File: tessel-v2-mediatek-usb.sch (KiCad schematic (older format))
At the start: 35 parts, among them J901 USB_A_2_stack, U201 MT7620N, U901 AIC1528-0PSTR, U903 FE1.1, X901 12MHz

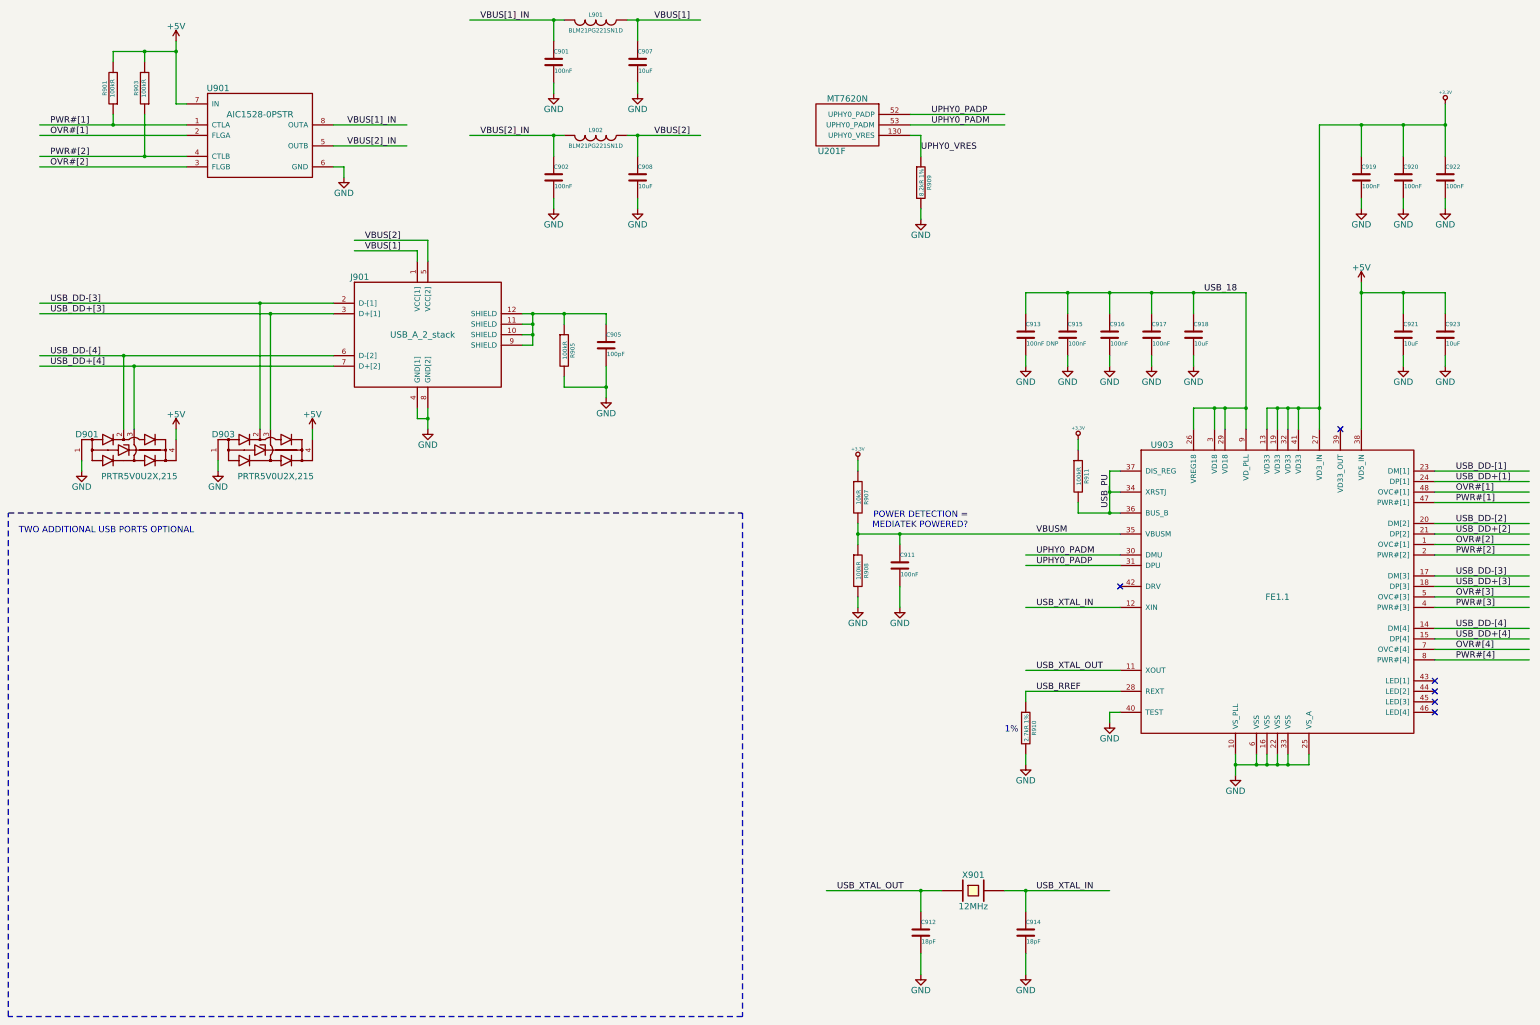
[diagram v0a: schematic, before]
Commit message: 1) can't believe i started from scratch 2) single best feature in today's kicad build: allign/distribute.
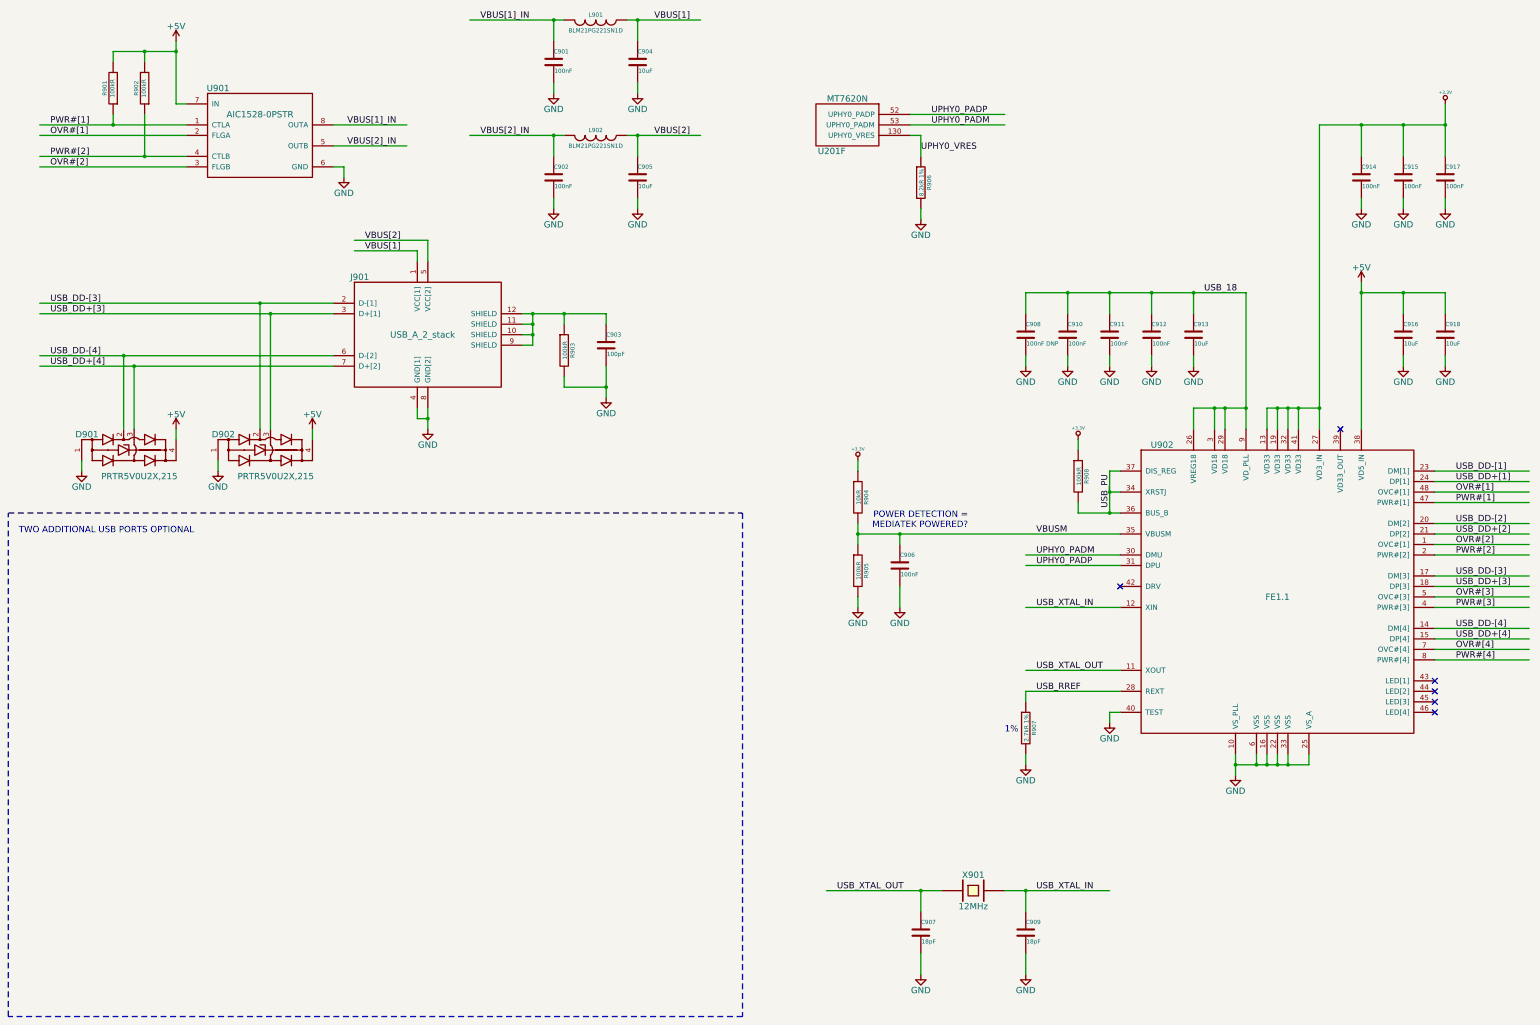
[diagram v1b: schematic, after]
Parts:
- renumbered C905 to C903, C907 to C904, C908 to C905, C911 to C906, C912 to C907, C913 to C908, C914 to C909, C915 to C910, C916 to C911, C917 to C912, C918 to C913, C919 to C914, C920 to C915, C921 to C916, C922 to C917, C923 to C918, D903 to D902, R903 to R902, R905 to R903, R907 to R904, R908 to R905, R909 to R906, R910 to R907, R911 to R908, U903 to U902

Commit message: sadly, we may need to rotate the mediatek...
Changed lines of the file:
@@
 $EndComp
 Text Label 1400 3600 0    60   ~ 0
-USB_DD-[3]
+USB_DD-[1]
 Text Label 1400 3700 0    60   ~ 0
-USB_DD+[3]
+USB_DD+[1]
 Text Label 1400 4100 0    60   ~ 0
-USB_DD-[4]
+USB_DD-[2]
 Text Label 1400 4200 0    60   ~ 0
-USB_DD+[4]
+USB_DD+[2]
 $Comp
 L PRTR5V0U2X,215 D901

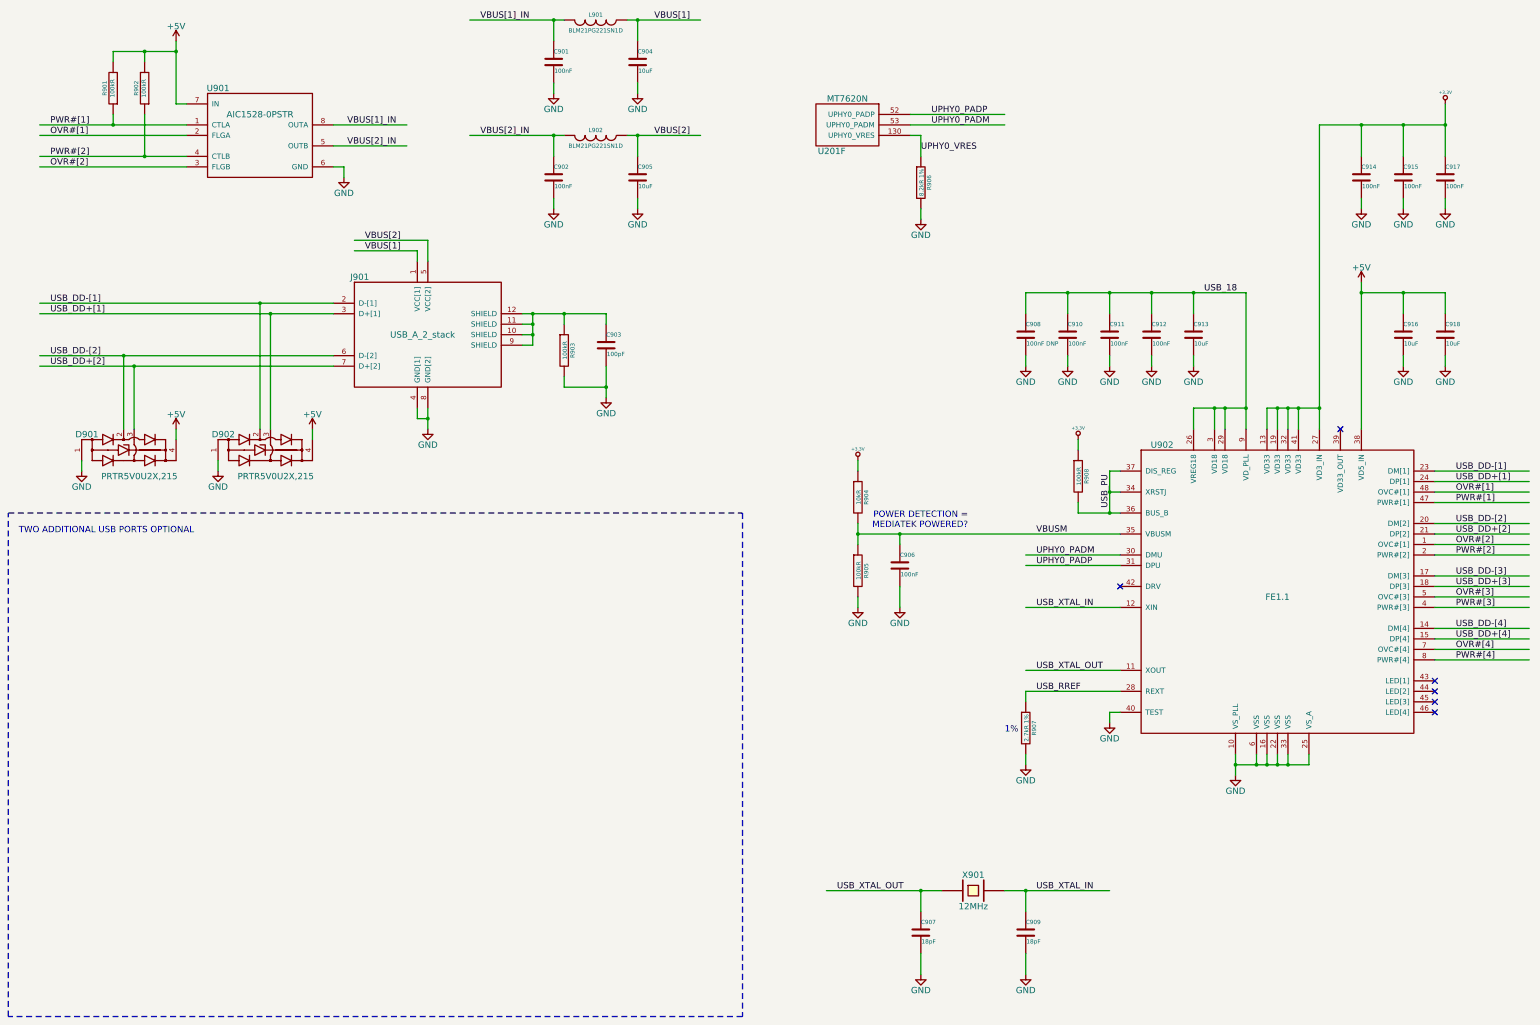
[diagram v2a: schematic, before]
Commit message: changes to usb domain: enable 3V3 reg, tie vbusm to mt33
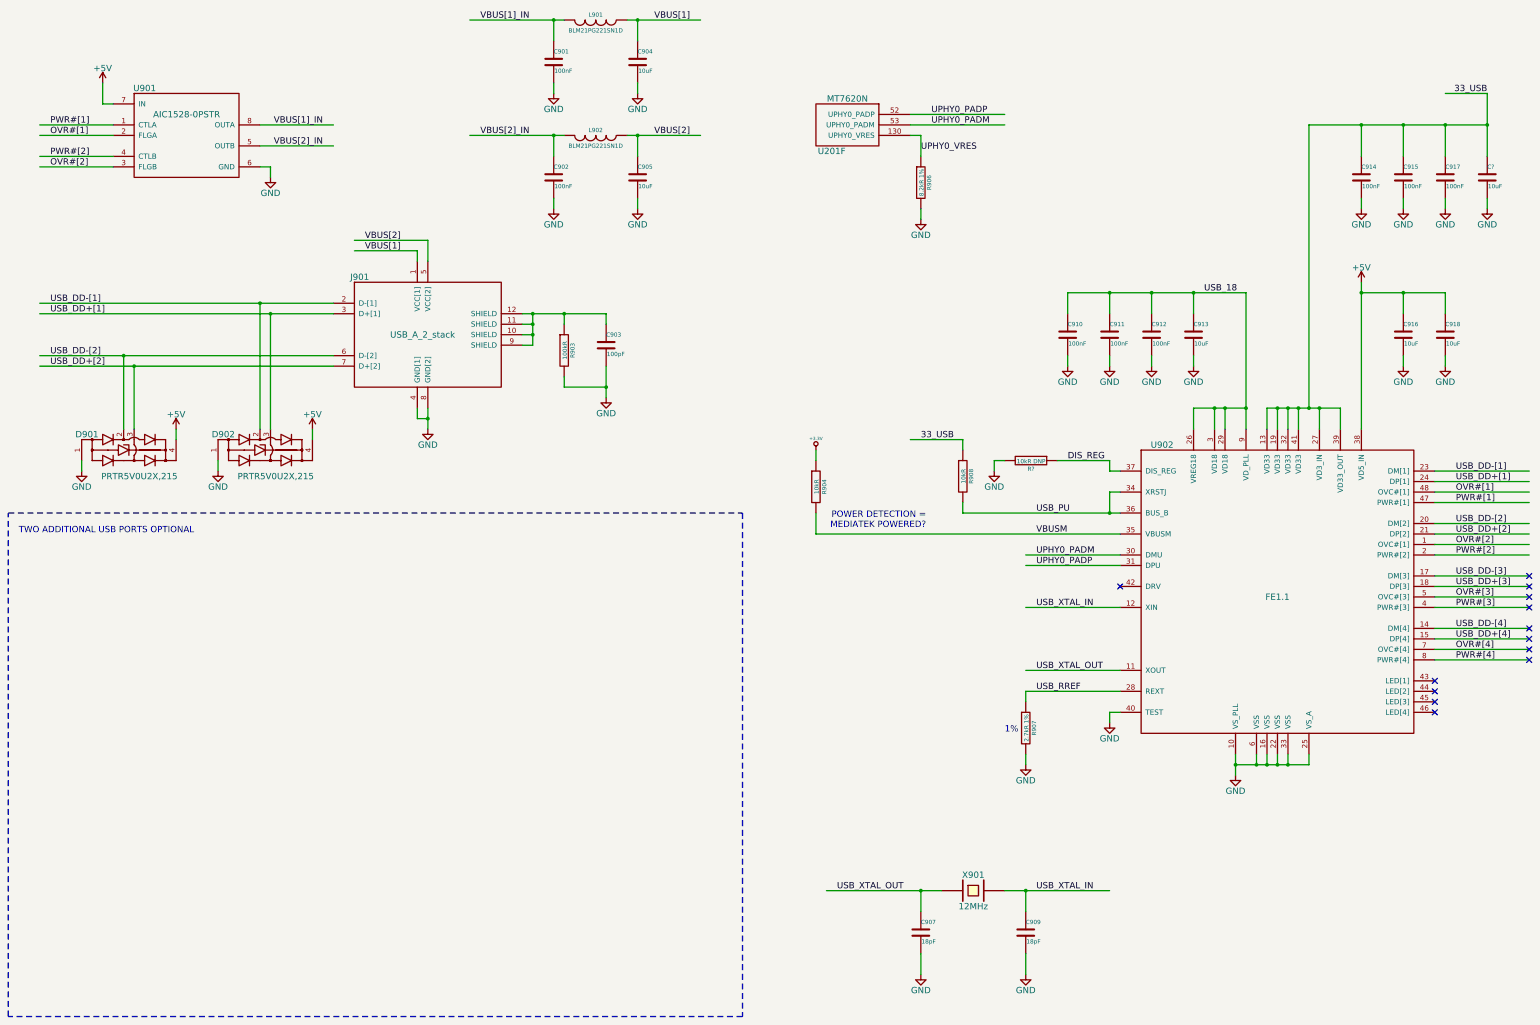
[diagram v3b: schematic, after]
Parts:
- removed C906: 100nF, tm-kicad-lib:SMD-0402-C, symbol C
- removed C908: 100nF DNP, tm-kicad-lib:SMD-0402-C, symbol C
- removed R901, R902, R905: 100kR, tm-kicad-lib:SMD-0402-R, symbol R
- added C?: 10uF, SMD_Packages:SMD-0805, symbol C
- added R?: 10kR DNP, tm-kicad-lib:SMD-0402-R, symbol R
- R908: value 100kR -> 10kR
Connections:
- net labels added: 33_USB, DIS_REG
- wire segments 146 -> 185
- no-connect marks 6 -> 13
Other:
- moved on the sheet: R904, R908, U901

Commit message: back-propogated componet information, placed lots of things
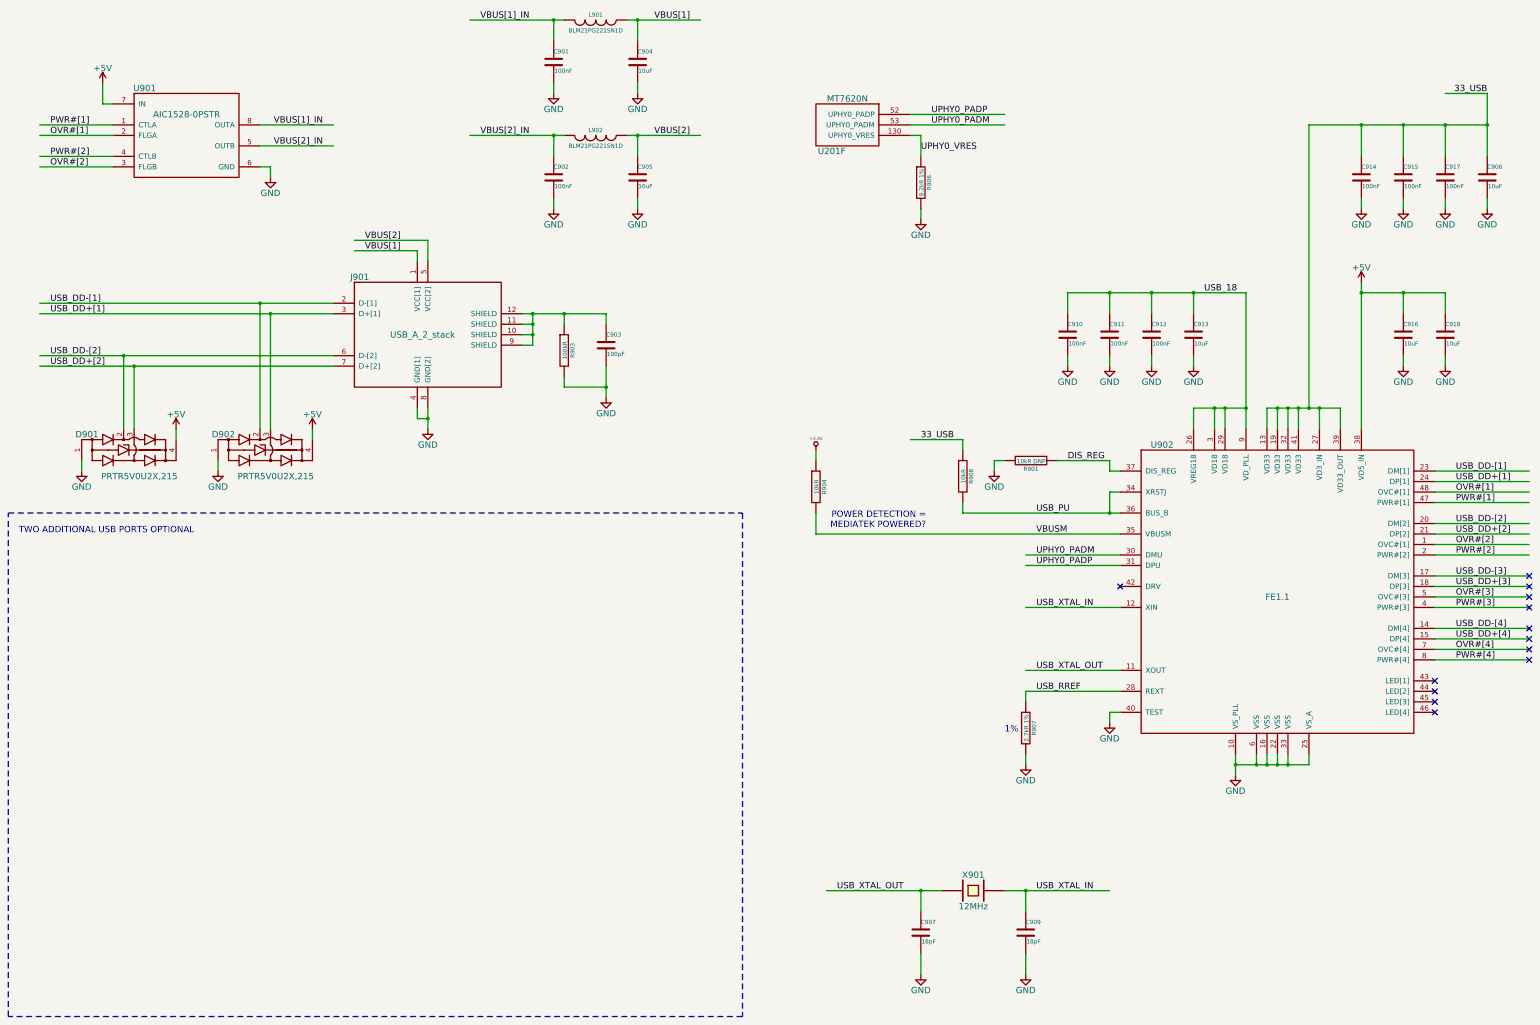
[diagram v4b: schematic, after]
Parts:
- C904, C905: footprint SMD_Packages:SMD-0805 -> tm-kicad-lib:SMD-0402-C
- C906: renamed from C?; footprint SMD_Packages:SMD-0805 -> tm-kicad-lib:SMD-0805-C
- C913, C916, C918: footprint SMD_Packages:SMD-0805 -> tm-kicad-lib:SMD-0805-C
- L901, L902: footprint SMD_Packages:SMD-0805 -> tm-kicad-lib:SMD-0805-R
- gave numbers to parts that had none: 1
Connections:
- wire segments 185 -> 146

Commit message: placement completele! let the routing begin!
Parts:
- C904, C905: footprint tm-kicad-lib:SMD-0402-C -> tm-kicad-lib:SMD-0805-C
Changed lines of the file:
@@
 F 0 "C905" H 7000 2500 40  0000 L CNN
 F 1 "10uF" H 7006 2315 40  0000 L CNN
-F 2 "tm-kicad-lib:SMD-0402-C" H 7038 2250 30  0001 C CNN
+F 2 "tm-kicad-lib:SMD-0805-C" H 7038 2250 30  0001 C CNN
 F 3 "" H 7000 2400 60  0000 C CNN
 	1    7000 2400
@@
 F 0 "C904" H 7000 1400 40  0000 L CNN
 F 1 "10uF" H 7006 1215 40  0000 L CNN
-F 2 "tm-kicad-lib:SMD-0402-C" H 7038 1150 30  0001 C CNN
+F 2 "tm-kicad-lib:SMD-0805-C" H 7038 1150 30  0001 C CNN
 F 3 "" H 7000 1300 60  0000 C CNN
 	1    7000 1300
